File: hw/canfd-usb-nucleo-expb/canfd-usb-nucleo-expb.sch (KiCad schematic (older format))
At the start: 58 parts, among them CN1 POWER, CN2 CONN, J1 USB_C_Receptacle_USB2.0, J2 Conn_01x10, J3 Conn_01x10, J4 Conn_01x10, SW1 SW_Push_Dual_x2, SW2 SW_Push_Dual_x2, SW3 SW_Push_Dual_x2, U1 USBLC6-2SC6, U2 ATA6561-GAQW-N, U3 ATA6561-GAQW-N, U4 ATA6561-GAQW-N

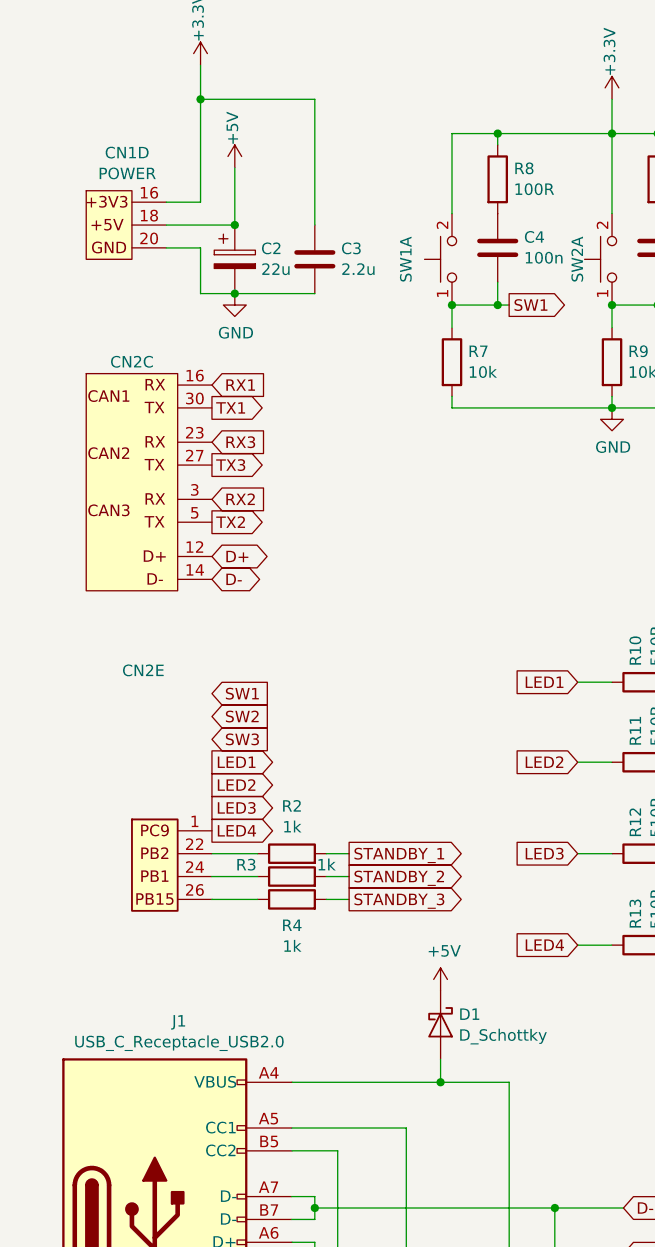
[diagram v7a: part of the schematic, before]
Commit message: HW: PCB layout is ready to review
Co-authored-by: Viacheslav Olizarenko <stiwenss@gmail.com>
Co-authored-by: AlexeyZ <silkt207@gmail.com>
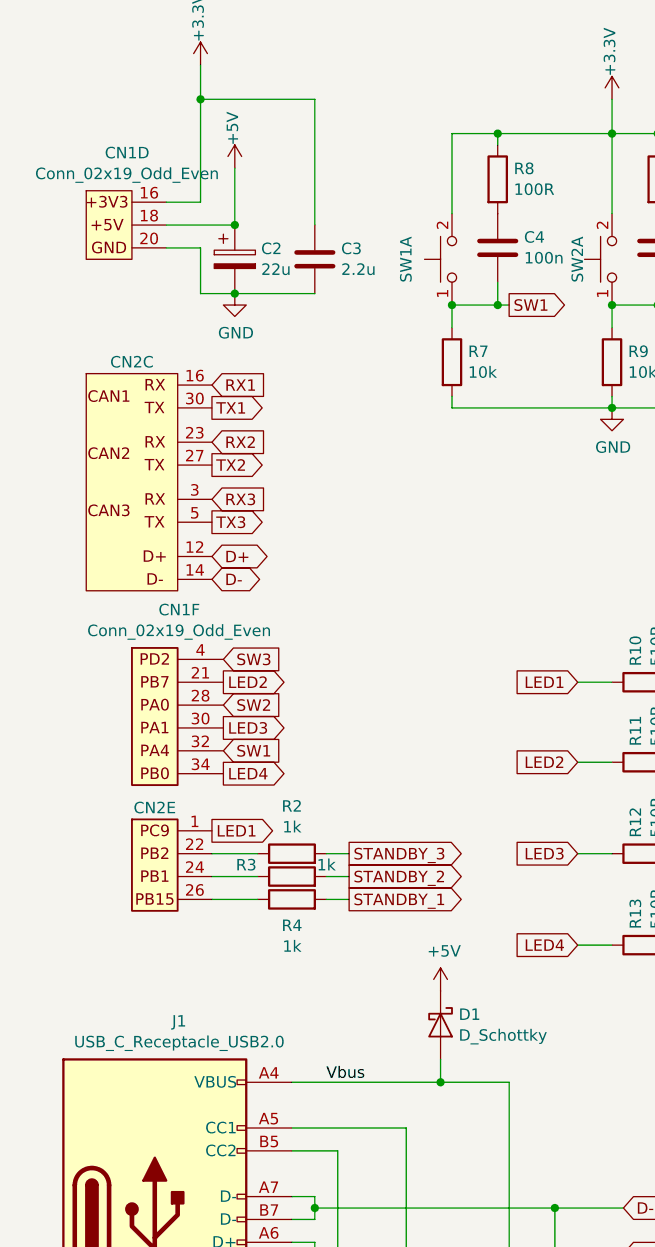
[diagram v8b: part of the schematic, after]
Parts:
- added unit 6 of CN1
- C2: footprint Capacitors_SMD:C_0805_HandSoldering -> Capacitor_SMD:C_1206_3216Metric
- CN1: value POWER -> Conn_02x19_Odd_Even
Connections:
- net LED1: now also CN2.1 (Pin_1)
- net LED2: now also CN1.21 (PB7)
- net LED3: now also CN1.30 (PA1)
- net LED4: now also CN1.34 (PB0); no longer CN2.1 (Pin_1)
- net RX2: now also CN2.23 (Pin_30); no longer CN2.3 (rx3)
- net RX3: now also CN2.3 (rx3); no longer CN2.23 (Pin_30)
- net STANDBY_1: now also R4.2; no longer R2.2
- net STANDBY_3: now also R2.2; no longer R4.2
- net SW1: now also CN1.32 (PA4)
- net SW2: now also CN1.28 (PA0)
- net SW3: now also CN1.4 (PD2)
- net TX2: now also CN2.27 (Pin_30); no longer CN2.5 (tx3)
- net TX3: now also CN2.5 (tx3); no longer CN2.27 (Pin_30)
- net Vbus: now reaches D1.2 (A), J1.A4 (VBUS), J1.A9 (VBUS), J1.B4 (VBUS), J1.B9 (VBUS), U1.5
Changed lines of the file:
@@
 Wire Wire Line
 	5250 2050 5500 2050
+Text GLabel 1350 2900 2    50   Output ~ 0
+TX3
+Text GLabel 1350 2300 2    50   Input ~ 0
+RX1
 Text GLabel 1350 2400 2    50   Output ~ 0
 TX1
 Text GLabel 1350 2550 2    50   Input ~ 0
-RX3
+RX2
 Text GLabel 1350 2650 2    50   Output ~ 0
-TX3
-Text GLabel 1350 2800 2    50   Input ~ 0
-RX2
-Text GLabel 1350 2900 2    50   Output ~ 0
 TX2
 Text GLabel 1350 3150 2    50   BiDi ~ 0
@@
 P 900 1600
 F 0 "CN1" H 979 1915 50  0000 C CNN
-F 1 "POWER" H 979 1824 50  0000 C CNN
+F 1 "Conn_02x19_Odd_Even" H 979 1824 50  0000 C CNN
 F 2 "Pin_Headers:Pin_Header_Straight_2x19_Pitch2.54mm" H 400 1150 50  0001 C CNN
 F 3 "" H 400 1150 50  0001 C CNN
@@
 	1    0    0    -1
 $EndComp
-Text GLabel 1350 2300 2    50   Input ~ 0
-RX1
+Text GLabel 1350 2800 2    50   Input ~ 0
+RX3
 Text GLabel 3350 1950 2    50   Output ~ 0
 SW2
@@
 U 5 1 5E62EF55
 P 1050 4550
-F 0 "CN2" H 1050 5550 50  0000 C CNN
+F 0 "CN2" H 1100 4950 50  0000 C CNN
 F 1 "CONN" H 1132 5576 50  0001 C CNN
 F 2 "Pin_Headers:Pin_Header_Straight_2x19_Pitch2.54mm" H 2100 4850 50  0001 C CNN
@@
 	1    0    0    -1
 $EndComp
-Text GLabel 1350 3650 2    50   Input ~ 0
+Text GLabel 1400 3900 2    50   Input ~ 0
 SW1
-Text GLabel 1350 3750 2    50   Input ~ 0
+Text GLabel 1400 3700 2    50   Input ~ 0
 SW2
-Text GLabel 1350 3850 2    50   Input ~ 0
+Text GLabel 1400 3500 2    50   Input ~ 0
 SW3
-Text GLabel 1350 3950 2    50   Output ~ 0
+Text GLabel 1350 4250 2    50   Output ~ 0
 LED1
-Text GLabel 1350 4050 2    50   Output ~ 0
+Text GLabel 1400 3600 2    50   Output ~ 0
 LED2
-Text GLabel 1350 4150 2    50   Output ~ 0
+Text GLabel 1400 3800 2    50   Output ~ 0
 LED3
-Text GLabel 1350 4250 2    50   Output ~ 0
+Text GLabel 1400 4000 2    50   Output ~ 0
 LED4
 Text GLabel 2950 3600 0    50   Input ~ 0
@@
 	5250 2200 5500 2200
 Text GLabel 1950 4550 2    50   Output ~ 0
-STANDBY_3
+STANDBY_1
 Text GLabel 1950 4450 2    50   Output ~ 0
 STANDBY_2
 Text GLabel 1950 4350 2    50   Output ~ 0
-STANDBY_1
+STANDBY_3
 Wire Wire Line
 	7100 3650 7350 3650
@@
 F 0 "C2" H 1565 1796 50  0000 L CNN
 F 1 "22u" H 1565 1705 50  0000 L CNN
-F 2 "Capacitors_SMD:C_0805_HandSoldering" H 1488 1600 50  0001 C CNN
+F 2 "Capacitor_SMD:C_1206_3216Metric" H 1488 1600 50  0001 C CNN
 F 3 "~" H 1450 1750 50  0001 C CNN
 	1    1450 1750
@@
 Wire Wire Line
 	2850 5900 3150 5900
+$Comp
+L canfd-usb-nucleo:Conn_02x19_Odd_Even CN1
+U 6 1 5E95CC46
+P 1100 3750
+F 0 "CN1" H 1207 4216 50  0000 C CNN
+F 1 "Conn_02x19_Odd_Even" H 1207 4125 50  0000 C CNN
+F 2 "Pin_Headers:Pin_Header_Straight_2x19_Pitch2.54mm" H 2150 4050 50  0001 C CNN
+F 3 "" H 2150 4050 50  0001 C CNN
+	6    1100 3750
+	1    0    0    -1
+$EndComp
+Text Label 1850 5350 0    50   ~ 0
+Vbus
 $EndSCHEMATC
